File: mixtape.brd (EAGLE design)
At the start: 95.1 x 39.1 mm, 54 parts, among them Q1 BSS123, SW1 WIREPADSMD1,27-254, SW2 WIREPADSMD1,27-254, U1 MCP73831, U5 ATMEGA32U4, U6 MIC5219-3.3, X1 MJ4435-R1503_03, X2 USB_MICROB_PLUGCONN-11752, Y2 8MHz

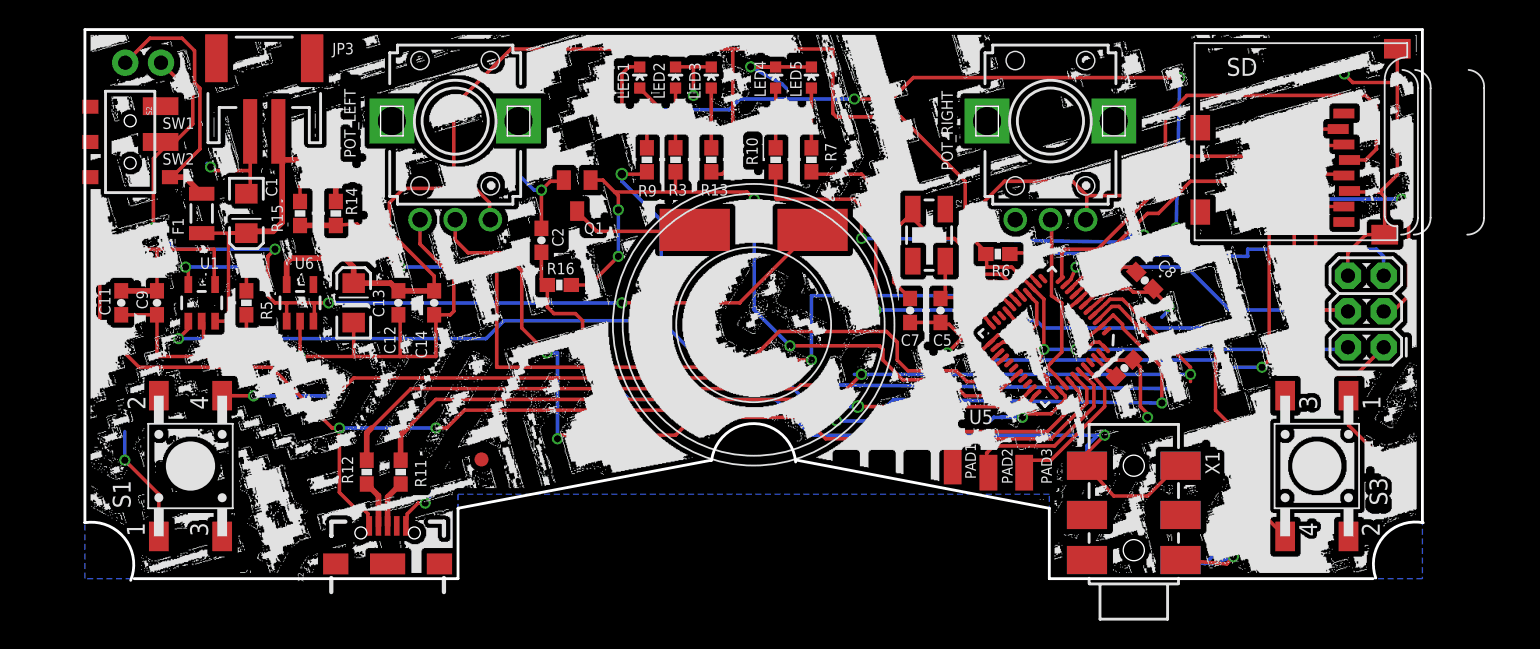
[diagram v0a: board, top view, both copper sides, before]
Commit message: Production Verions
Added repot to https://kitnic.it/ with 1-click BOM
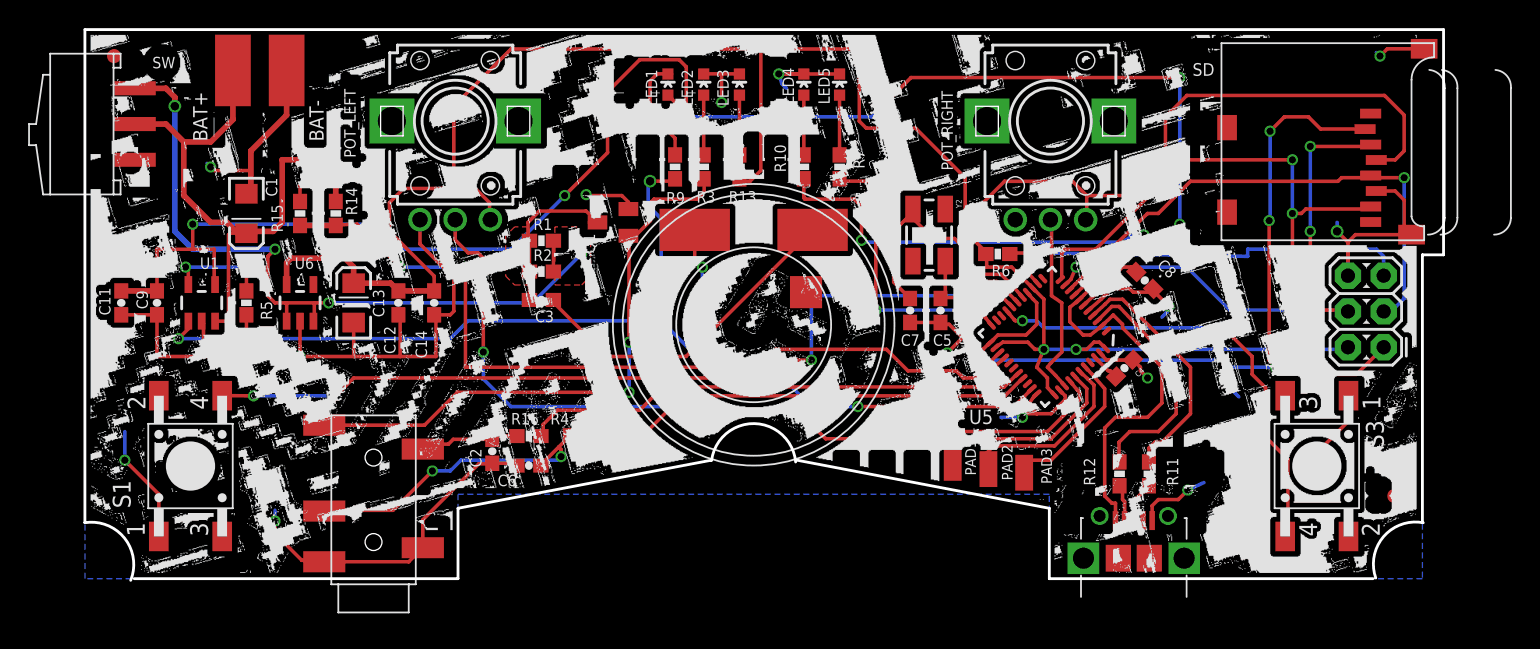
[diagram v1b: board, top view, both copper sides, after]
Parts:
- removed F1: PTCSMD, SparkFun:PTC-1206
- removed JP10: FIDUCIALUFIDUCIAL, SparkFun:FIDUCIAL-1X2
- removed JP3: (no value), SparkFun:JST-2-SMD
- removed JP7: External Switch, SparkFun:1X02
- removed S2: Power Switch, SparkFun:AYZ0202
- removed SW1, SW2: WIREPADSMD1,27-254, wirepad:SMD1,27-2,54
- added BAT+, BAT-: (no value), wirepad:SMD2,54-5,08
- added C3, C6: 1uF, SparkFun-Capacitors:0603-CAP
- added R1, R2: 33, SparkFun-Resistors:0603-RES
- added R4: 330, SparkFun-Resistors:0603-RES
- added SW: SWITCH_SMD, Gaudi:SWITCH_SMD
- added U$1, U$2: FIDUCIAL, adafruit:FIDUCIAL_1MM
- X1: value MJ4435-R1503_03 -> USB_B_SMD; device Gaudi:1503_02 -> Gaudi:USB_B_SMD
- X2: value USB_MICROB_PLUGCONN-11752 -> PJ-327A; device SparkFun-Connectors:USB-B-MICRO-SMD_V03 -> Gaudi:PJ-327A
- moved R12 53.5 mm to (76.0, 9.45)
- moved R11 53.1 mm to (78.1, 9.45)
- moved U$4 40.4 mm to (88.4, 34.5)
- moved LOGO1 18.2 mm to (82.8, 10.8)
- moved C2 15.4 mm to (31.4, 11.0), turned to 90 degrees
- moved R16 10.9 mm to (34.0, 12.1)
- moved X1 4.60 mm to (77.0, 6.13), turned to 0 degrees
- moved Q1 3.18 mm to (40.0, 27.3), turned to 90 degrees
- moved LED1 2.06 mm to (43.9, 37.1)
- moved LED2 2.06 mm to (46.5, 37.1)
- moved LED3 2.06 mm to (49.0, 37.1)
- moved LED4 2.06 mm to (53.6, 37.1)
- moved LED5 2.06 mm to (56.1, 37.1)
- moved R10 2.06 mm to (53.6, 31.2)
- moved R13 2.06 mm to (49.0, 31.2)
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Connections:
- removed net N$13: Q1.3, SPEAKER.2
- removed net N$9: F1.2, JP7.2, S2.3
- new net N$2: C3.2, Q1.3, R1.1, R2.1
- new net N$3: C3.1, SPEAKER.1
- new net N$4: C6.2, R4.1, X2.3
- new net N$7: Q1.1, R3.2, X2.4
- net D10: now also R4.2
- net D9: no longer Q1.1, R3.2
- net GND: now also BAT-.1, C6.1, SPEAKER.2, X1.GND, X2.1, X2.5; no longer JP3.1, X1.1, X1.11B, X1.1B, X2.GND1
- net MISO: now also SD.7; no longer SD.3
- net MOSI: now also SD.3; no longer SD.7
- net N$20: now also X1.D-; no longer X2.D-1
- net N$21: now also X2.2; no longer X1.3, X1.33, X1.33B
- net N$5: now also X1.D+; no longer X2.D+1
- net RAW: now also R1.2, R2.2, SW.S1; no longer JP7.1, S2.2, SPEAKER.1
- net USB_VCC: now also X1.VCC; no longer X2.VBUS
- net VBATT: now also BAT+.1, SW.COM; no longer F1.1, JP3.2
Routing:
- net N$21: track 62.4 -> 7.07 mm, vias 2 -> 0
- net D+: track 70.6 -> 17.6 mm, vias 2 -> 0
- net D-: track 70.2 -> 17.5 mm, vias 2 -> 0
- net N$7: track 0.00 -> 42.1 mm, vias 0 -> 2
- net USB_VCC: track 183.1 -> 145.0 mm, vias 8 -> 6
- net D10: track 0.00 -> 32.1 mm
- net N$3: track 0.00 -> 23.9 mm
- net N$4: track 0.00 -> 22.8 mm, vias 0 -> 2
- net RAW: track 71.7 -> 52.6 mm
- net N$9: track 18.9 -> 0.00 mm
- net D9: track 52.7 -> 36.1 mm, vias 4 -> 0
- net VBATT: track 27.6 -> 42.5 mm
- net N$2: track 0.00 -> 11.6 mm
- net GND: track 180.2 -> 189.5 mm, vias 15 -> 17
- net N$13: track 9.02 -> 0.00 mm
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- added copper zone on layer 1, net N$2
- added copper zone on layer 1, net RAW
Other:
- board size 95.1 x 39.1 mm -> 96.5 x 39.1 mm
- board text added: "PRODUCED AT R2 MANUFACTURING, SWITZERLAND"
- board text added: "Version 1.0, 2016"
- board text removed: "Version 0.1, 2014"

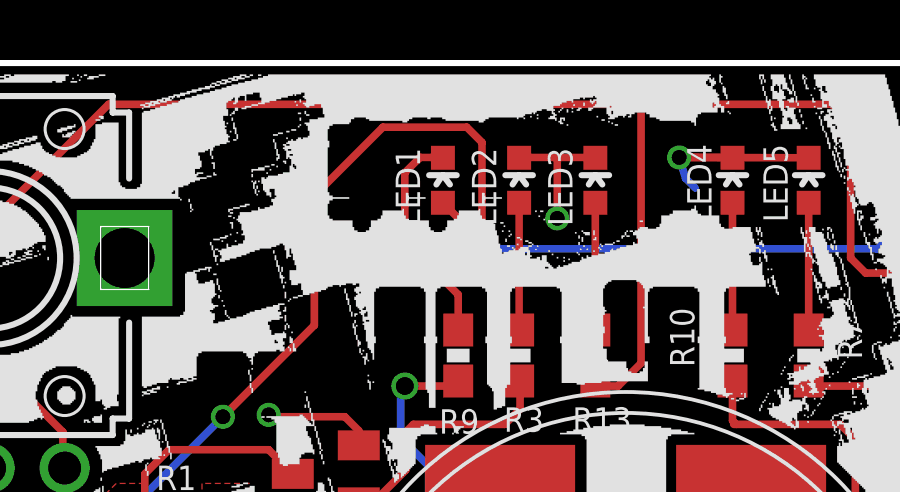
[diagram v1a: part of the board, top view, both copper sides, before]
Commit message: corected error on USB port in BOM
plus minor updates
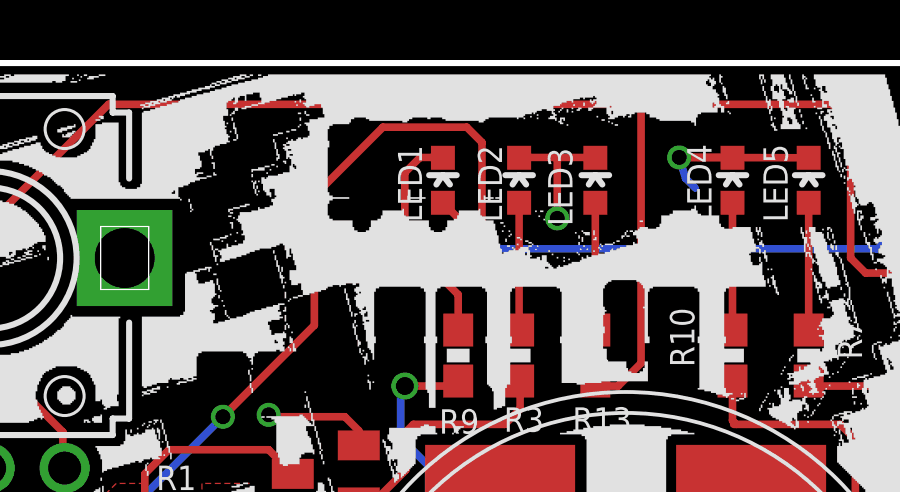
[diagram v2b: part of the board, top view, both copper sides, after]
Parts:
- LED2: value Red -> Blue
- LED3: value Red -> Green
- LED4: value Blue -> Red
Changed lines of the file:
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@@
 <attribute name="NAME" x="45.942" y="28.71" size="0.8128" layer="25" font="vector" ratio="15"/>
 </element>
-<element name="LED2" library="SparkFun" package="LED-0603" value="Red" x="46.45" y="37.092" smashed="yes">
-<attribute name="NAME" x="45.688" y="35.568" size="0.8128" layer="25" font="vector" ratio="15" rot="R90"/>
+<element name="LED2" library="SparkFun" package="LED-0603" value="Blue" x="46.45" y="37.092" smashed="yes">
+<attribute name="NAME" x="45.8785" y="35.695" size="0.8" layer="25" font="vector" ratio="15" rot="R90"/>
+<attribute name="VALUE" x="47.4025" y="36.33" size="0.4064" layer="27" rot="R90"/>
 </element>
 <element name="C9" library="SparkFun-Capacitors" package="0603-CAP" value="4.7uF" x="7.62" y="21.59" smashed="yes" rot="R270">
@@
 </element>
 <element name="LED1" library="SparkFun" package="LED-0603" value="Yellow" x="43.91" y="37.092" smashed="yes">
-<attribute name="NAME" x="43.148" y="35.568" size="0.8128" layer="25" font="vector" ratio="15" rot="R90"/>
+<attribute name="NAME" x="43.2115" y="35.695" size="0.8" layer="25" font="vector" ratio="15" rot="R90"/>
+<attribute name="VALUE" x="44.7355" y="36.203" size="0.4064" layer="27" rot="R90"/>
 </element>
 <element name="R9" library="SparkFun-Resistors" package="0603-RES" value="470" x="44.418" y="31.25" smashed="yes" rot="R90">
@@
 <attribute name="VALUE" x="54.705" y="30.234" size="0.4064" layer="27" font="vector" rot="R90"/>
 </element>
-<element name="LED4" library="SparkFun" package="LED-0603" value="Blue" x="53.562" y="37.092" smashed="yes">
+<element name="LED4" library="SparkFun" package="LED-0603" value="Red" x="53.562" y="37.092" smashed="yes">
 <attribute name="NAME" x="52.8635" y="35.695" size="0.8128" layer="25" font="vector" ratio="15" rot="R90"/>
-<attribute name="VALUE" x="54.6415" y="36.076" size="0.4064" layer="27" rot="R90"/>
+<attribute name="VALUE" x="54.5145" y="36.584" size="0.4064" layer="27" rot="R90"/>
 </element>
 <element name="R11" library="SparkFun-Resistors" package="0603-RES" value="22" x="78.0745" y="9.4455" smashed="yes" rot="R270">
@@
 <attribute name="VALUE" x="47.847" y="32.266" size="0.4064" layer="27" font="vector" rot="R270"/>
 </element>
-<element name="LED3" library="SparkFun" package="LED-0603" value="Red" x="48.99" y="37.092" smashed="yes">
+<element name="LED3" library="SparkFun" package="LED-0603" value="Green" x="48.99" y="37.092" smashed="yes">
 <attribute name="NAME" x="48.228" y="35.568" size="0.8128" layer="25" font="vector" ratio="15" rot="R90"/>
 <attribute name="VALUE" x="50.0695" y="36.076" size="0.4064" layer="27" rot="R90"/>
